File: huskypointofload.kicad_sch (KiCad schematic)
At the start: 8 parts, among them J1 POWER, J2 RFSOC_POWER

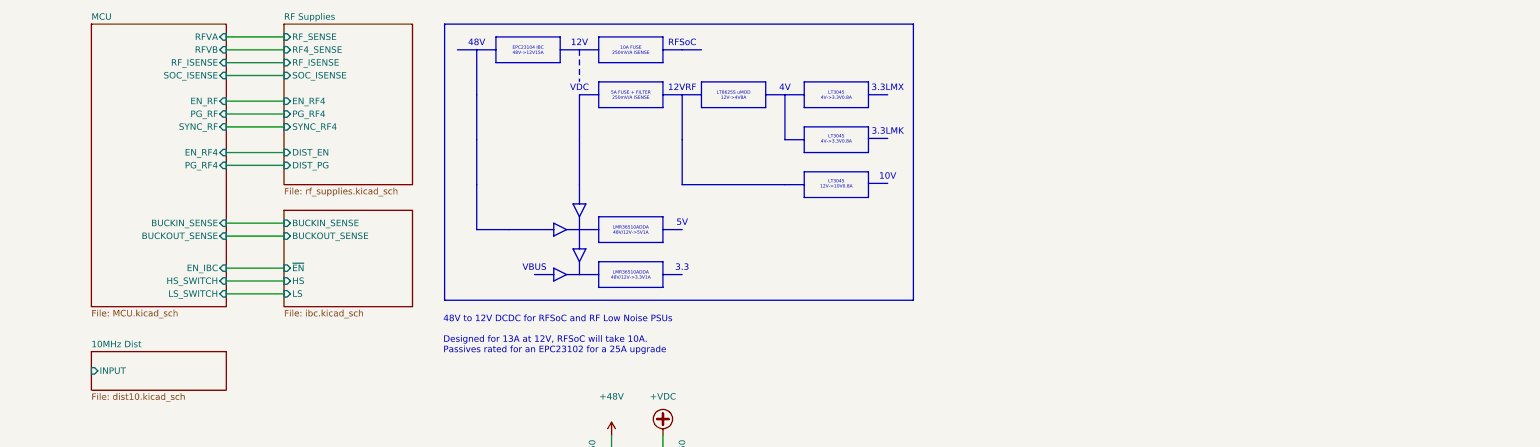
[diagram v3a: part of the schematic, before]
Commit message: Add lmk and bump schematic size
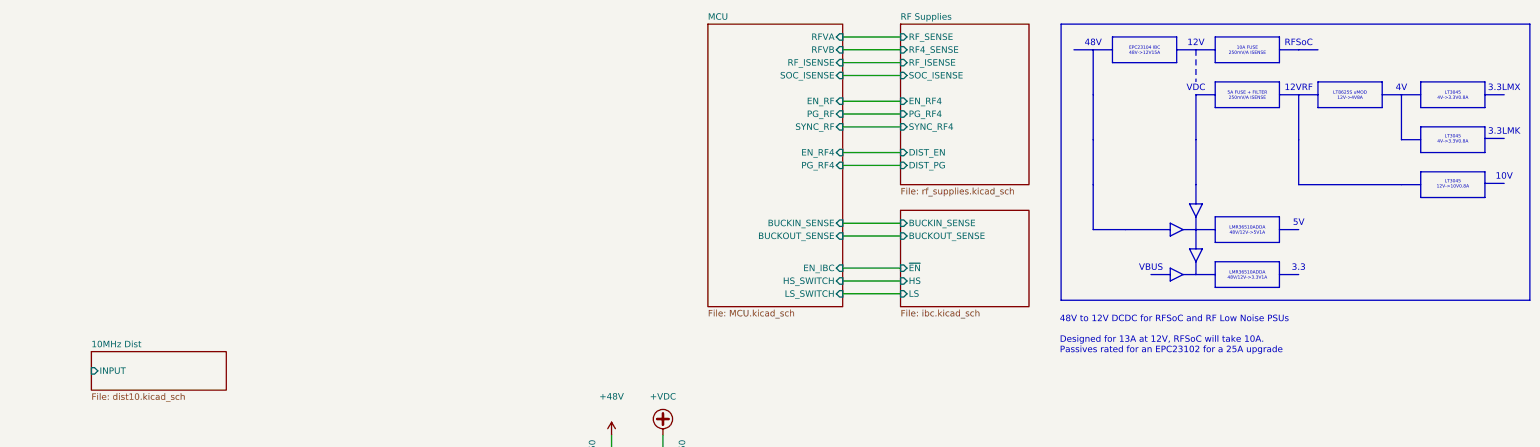
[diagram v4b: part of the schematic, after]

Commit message: Add LMX Draft
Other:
- note added: "3.3LMKDIG"
- note added: "3.3LMKVCO"
- note added: "3.3LMXDIG"
- note added: "3.3LMXPLL"
- note added: "3.3LMXVCO"
- note removed: "3.3LMK"
- note removed: "3.3LMX"

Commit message: Different Matching Circuit
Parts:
- added J39: 10MHZ, symbol Connector:Conn_Coaxial_Small
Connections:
- net 10MHz Dist/INPUT: now also J39.1 (In)
- net GND: now also J39.2 (Ext)
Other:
- sheet Clocking ports: added BACKUP_DIS, LD1, LD2, LD_LED_ENABLE, LMKRESET, LMXCE, MUXOUT, OUTA, OUTB, RAMPCLK, RAMPDIR, SCK, SDIO, SEL0, SEL1, ~{LMKCS}, ~{LMXCS}; removed none
- sheet MCU ports: added BACKUP_DIS, LD1, LD2, LMKRESET, LMXCE, LOCK_LEDS, MISO, MOSI, RAMPCLK, RAMPDIR, SCK, SEL0, SEL1, ~{LMKCS}, ~{LMXCS}; removed none
- moved on the sheet: D1, D2, D3, D4, R1, R2

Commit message: Add mixer
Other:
- added sheet TX Mixer (hmc525.kicad_sch)
- moved on the sheet: J39
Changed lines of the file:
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@@
 	(wire
 		(pts
-			(xy 171.45 95.25) (xy 171.45 97.79)
+			(xy 331.47 29.21) (xy 331.47 31.75)
 		)
 		(stroke
@@
 	(wire
 		(pts
-			(xy 171.45 87.63) (xy 177.8 87.63)
+			(xy 331.47 21.59) (xy 325.12 21.59)
 		)
 		(stroke
@@
 	(wire
 		(pts
-			(xy 171.45 87.63) (xy 171.45 90.17)
+			(xy 331.47 21.59) (xy 331.47 24.13)
 		)
 		(stroke
@@
 	(symbol
 		(lib_id "power:GND")
-		(at 171.45 97.79 0)
+		(at 331.47 31.75 0)
+		(mirror y)
 		(unit 1)
 		(exclude_from_sim no)
@@
 		(fields_autoplaced yes)
 		(property "Reference" "#PWR0263"
-			(at 171.45 104.14 0)
+			(at 331.47 38.1 0)
 			(effects
 				(font
@@
 		)
 		(property "Value" "GND"
-			(at 171.45 102.87 0)
+			(at 331.47 36.83 0)
 			(effects
 				(font
@@
 		)
 		(property "Footprint" ""
-			(at 171.45 97.79 0)
+			(at 331.47 31.75 0)
 			(effects
 				(font
@@
 		)
 		(property "Datasheet" ""
-			(at 171.45 97.79 0)
+			(at 331.47 31.75 0)
 			(effects
 				(font
@@
 		)
 		(property "Description" "Power symbol creates a global label with name \"GND\" , ground"
-			(at 171.45 97.79 0)
+			(at 331.47 31.75 0)
 			(effects
 				(font
@@
 	(symbol
 		(lib_id "Connector:Conn_Coaxial_Small")
-		(at 171.45 92.71 270)
+		(at 331.47 26.67 90)
+		(mirror x)
 		(unit 1)
 		(exclude_from_sim no)
@@
 		(dnp no)
 		(property "Reference" "J39"
-			(at 168.91 90.9203 90)
+			(at 334.01 24.8803 90)
 			(effects
 				(font
@@
 		)
 		(property "Value" "10MHZ"
-			(at 168.91 93.4603 90)
+			(at 334.01 27.4203 90)
 			(effects
 				(font
@@
 		)
 		(property "Footprint" ""
-			(at 171.45 92.71 0)
+			(at 331.47 26.67 0)
 			(effects
 				(font
@@
 		)
 		(property "Datasheet" "~"
-			(at 171.45 92.71 0)
+			(at 331.47 26.67 0)
 			(effects
 				(font
@@
 		)
 		(property "Description" "small coaxial connector (BNC, SMA, SMB, SMC, Cinch/RCA, LEMO, ...)"
-			(at 171.45 92.71 0)
+			(at 331.47 26.67 0)
 			(effects
 				(font
@@
 	)
 	(sheet
-		(at 177.8 83.82)
-		(size 31.75 7.62)
+		(at 298.45 17.78)
+		(size 26.67 7.62)
 		(exclude_from_sim no)
 		(in_bom yes)
@@
 		)
 		(property "Sheetname" "10MHz Dist"
-			(at 177.8 83.1084 0)
+			(at 298.45 17.0684 0)
 			(effects
 				(font
@@
 		)
 		(property "Sheetfile" "dist10.kicad_sch"
-			(at 177.8 92.0246 0)
+			(at 298.45 25.9846 0)
 			(effects
 				(font
@@
 		)
 		(pin "INPUT" input
-			(at 177.8 87.63 180)
+			(at 325.12 21.59 0)
 			(effects
 				(font
 					(size 1.27 1.27)
 				)
-				(justify left)
+				(justify right)
 			)
 		)
@@
 				)
 			)
+		)
+	)
+	(sheet
+		(at 177.8 83.82)
+		(size 25.4 10.16)
+		(exclude_from_sim no)
+		(in_bom yes)
+		(on_board yes)
+		(dnp no)
+		(fields_autoplaced yes)
+		(stroke
+			(width 0.1524)
+			(type solid)
+		)
+		(fill
+			(color 0 0 0 0.0000)
+		)
+		(property "Sheetname" "TX Mixer"
+			(at 177.8 83.1084 0)
+			(effects
+				(font
+					(size 1.27 1.27)
+				)
+				(justify left bottom)
+			)
+		)
+		(property "Sheetfile" "hmc525.kicad_sch"
+			(at 177.8 94.5646 0)
+			(effects
+				(font
+					(size 1.27 1.27)
+				)
+				(justify left top)
+			)
+		)
+		(pin "I" input
+			(at 203.2 86.36 0)
+			(effects
+				(font
+					(size 1.27 1.27)
+				)
+				(justify right)
+			)
+		)
+		(pin "LO" input
+			(at 177.8 86.36 180)
+			(effects
+				(font
+					(size 1.27 1.27)
+				)
+				(justify left)
+			)
+		)
+		(pin "Q" input
+			(at 203.2 88.9 0)
+			(effects
+				(font
+					(size 1.27 1.27)
+				)
+				(justify right)
+			)
+		)
+		(pin "RF" input
+			(at 177.8 88.9 180)
+			(effects
+				(font
+					(size 1.27 1.27)
+				)
+				(justify left)
+			)
+		)
+		(pin "6V" input
+			(at 177.8 91.44 180)
+			(effects
+				(font
+					(size 1.27 1.27)
+				)
+				(justify left)
+			)
+		)
+		(instances
+			(project "huskypointofload"
+				(path "/eb9c972b-d134-41da-be97-ece3f463f7e0"
+					(page "34")
+				)
+			)

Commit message: WIP Splitrail
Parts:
- added U18: ADA4077-1xR, Package_SO:SOIC-8_3.9x4.9mm_P1.27mm, symbol Amplifier_Operational:ADA4077-1xR
- added U27: ADL8124, Package_CSP:LFCSP-8_2x2mm_P0.5mm, symbol huskylib:ADL8124
- added U28: LT3093xMSE, Package_SO:MSOP-12-1EP_3x4.039mm_P0.65mm_EP1.651x2.845mm, symbol Regulator_Linear:LT3093xMSE
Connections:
- new net: U28.1 (IN), U28.13 (IN), U28.2 (IN)
- new net: U28.11 (OUT), U28.12 (OUT)
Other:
- removed sheet Clocking
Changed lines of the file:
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@@
+	)
+	(symbol
+		(lib_id "Regulator_Linear:LT3093xMSE")
+		(at 132.08 138.43 0)
+		(unit 1)
+		(exclude_from_sim no)
+		(in_bom yes)
+		(on_board yes)
+		(dnp no)
+		(fields_autoplaced yes)
+		(property "Reference" "U28"
+			(at 132.08 125.73 0)
+			(effects
+				(font
+					(size 1.27 1.27)
+				)
+			)
+		)
+		(property "Value" "LT3093xMSE"
+			(at 132.08 128.27 0)
+			(effects
+				(font
+					(size 1.27 1.27)
+				)
+			)
+		)
+		(property "Footprint" "Package_SO:MSOP-12-1EP_3x4.039mm_P0.65mm_EP1.651x2.845mm"
+			(at 132.08 127.635 0)
+			(effects
+				(font
+					(size 1.27 1.27)
+				)
+				(hide yes)
+			)
+		)
+		(property "Datasheet" "https://www.analog.com/media/en/technical-documentation/data-sheets/lt3093.pdf"
+			(at 132.08 135.89 0)
+			(effects
+				(font
+					(size 1.27 1.27)
+				)
+				(hide yes)
+			)
+		)
+		(property "Description" "-200mA, Adjustable, Ultralow Noise, Ultrahigh PSRR RF Negative Linear Regulator, MSOP-12"
+			(at 132.08 138.43 0)
+			(effects
+				(font
+					(size 1.27 1.27)
+				)
+				(hide yes)
+			)
+		)
+		(pin "13"
+		)
+		(pin "12"
+		)
+		(pin "1"
+		)
+		(pin "2"
+		)
+		(pin "3"
+		)
+		(pin "4"
+		)
+		(pin "7"
+		)
+		(pin "8"
+		)
+		(pin "9"
+		)
+		(pin "11"
+		)
+		(pin "10"
+		)
+		(pin "5"
+		)
+		(pin "6"
+		)
+		(instances
+			(project ""
+				(path "/eb9c972b-d134-41da-be97-ece3f463f7e0"
+					(reference "U28")
+					(unit 1)
+				)
+			)
+		)
+	)
+	(symbol
+		(lib_id "huskylib:ADL8124")
+		(at 147.32 102.87 0)
+		(unit 1)
+		(exclude_from_sim no)
+		(in_bom yes)
+		(on_board yes)
+		(dnp no)
+		(fields_autoplaced yes)
+		(property "Reference" "U27"
+			(at 135.89 91.948 0)
+			(do_not_autoplace yes)
+			(effects
+				(font
+					(size 1.27 1.27)
+				)
+				(justify left bottom)
+			)
+		)
+		(property "Value" "ADL8124"
+			(at 135.89 93.726 0)
+			(do_not_autoplace yes)
+			(effects
+				(font
+					(size 1.27 1.27)
+				)
+				(justify left bottom)
+			)
+		)
+		(property "Footprint" "Package_CSP:LFCSP-8_2x2mm_P0.5mm"
+			(at 147.32 102.87 0)
+			(effects
+				(font
+					(size 1.27 1.27)
+				)
+				(hide yes)
+			)
+		)
+		(property "Datasheet" "https://www.analog.com/media/en/technical-documentation/data-sheets/adl8124.pdf"
+			(at 147.32 102.87 0)
+			(effects
+				(font
+					(size 1.27 1.27)
+				)
+				(hide yes)
+			)
+		)
+		(property "Description" ""
+			(at 147.32 102.87 0)
+			(effects
+				(font
+					(size 1.27 1.27)
+				)
+				(hide yes)
+			)
+		)
+		(pin "4"
+		)
+		(pin "9"
+		)
+		(pin "4"
+		)
+		(pin "5"
+		)
+		(pin "7"
+		)
+		(pin "1"
+		)
+		(pin "3"
+		)
+		(pin "6"
+		)
+		(pin "8"
+		)
+		(pin "8"
+		)
+		(instances
+			(project ""
+				(path "/eb9c972b-d134-41da-be97-ece3f463f7e0"
+					(reference "U27")
+					(unit 1)
+				)
+			)
+		)
 	)
 	(symbol
@@
 		)
 	)
+	(symbol
+		(lib_id "Amplifier_Operational:ADA4077-1xR")
+		(at 231.14 119.38 0)
+		(unit 1)
+		(exclude_from_sim no)
+		(in_bom yes)
+		(on_board yes)
+		(dnp no)
+		(fields_autoplaced yes)
+		(property "Reference" "U18"
+			(at 243.84 112.9598 0)
+			(effects
+				(font
+					(size 1.27 1.27)
+				)
+			)
+		)
+		(property "Value" "ADA4077-1xR"
+			(at 243.84 115.4998 0)
+			(effects
+				(font
+					(size 1.27 1.27)
+				)
+			)
+		)
+		(property "Footprint" "Package_SO:SOIC-8_3.9x4.9mm_P1.27mm"
+			(at 228.6 124.46 0)
+			(effects
+				(font
+					(size 1.27 1.27)
+				)
+				(justify left)
+				(hide yes)
+			)
+		)
+		(property "Datasheet" "https://www.analog.com/media/en/technical-documentation/data-sheets/ADA4077-1_4077-2_4077-4.pdf"
+			(at 234.95 115.57 0)
+			(effects
+				(font
+					(size 1.27 1.27)
+				)
+				(hide yes)
+			)
+		)
+		(property "Description" "4MHz, 7nV/sqrtHz, Low Offset and Drift, High Precision Amplifier, SOIC-8"
+			(at 231.14 119.38 0)
+			(effects
+				(font
+					(size 1.27 1.27)
+				)
+				(hide yes)
+			)
+		)
+		(pin "6"
+		)
+		(pin "1"
+		)
+		(pin "5"
+		)
+		(pin "4"
+		)
+		(pin "3"
+		)
+		(pin "8"
+		)
+		(pin "7"
+		)
+		(pin "2"
+		)
+		(instances
+			(project ""
+				(path "/eb9c972b-d134-41da-be97-ece3f463f7e0"
+					(reference "U18")
+					(unit 1)
+				)
+			)
+		)
+	)
 	(sheet
 		(at 269.24 17.78)
@@
 				)
 			)
-		)
-	)
-	(sheet
-		(at 177.8 17.78)
-		(size 31.75 55.88)
-		(exclude_from_sim no)
-		(in_bom yes)
-		(on_board yes)
-		(dnp no)
-		(fields_autoplaced yes)
-		(stroke
-			(width 0.1524)
-			(type solid)
-		)
-		(fill
-			(color 0 0 0 0.0000)
-		)
-		(property "Sheetname" "Clocking"
-			(at 177.8 17.0684 0)
-			(effects
-				(font
-					(size 1.27 1.27)
-				)
-				(justify left bottom)
-			)
-		)
-		(property "Sheetfile" "clocking.kicad_sch"
-			(at 177.8 74.2446 0)
-			(effects
-				(font
-					(size 1.27 1.27)
-				)
-				(justify left top)
-			)
-		)
-		(pin "BACKUP_DIS" input
-			(at 209.55 53.34 0)
-			(effects
-				(font
-					(size 1.27 1.27)
-				)
-				(justify right)
-			)
-		)
-		(pin "LD1" input
-			(at 209.55 58.42 0)
-			(effects
-				(font
-					(size 1.27 1.27)
-				)
-				(justify right)
-			)
-		)
-		(pin "LD2" input
-			(at 209.55 60.96 0)
-			(effects
-				(font
-					(size 1.27 1.27)
-				)
-				(justify right)
-			)
-		)
-		(pin "LD_LED_ENABLE" input
-			(at 209.55 66.04 0)
-			(effects
-				(font
-					(size 1.27 1.27)
-				)
-				(justify right)
-			)
-		)
-		(pin "LMKRESET" input
-			(at 209.55 20.32 0)
-			(effects
-				(font
-					(size 1.27 1.27)
-				)
-				(justify right)
-			)
-		)
-		(pin "LMXCE" input
-			(at 209.55 22.86 0)
-			(effects
-				(font
-					(size 1.27 1.27)
-				)
-				(justify right)
-			)
-		)
-		(pin "MUXOUT" input
-			(at 209.55 63.5 0)
-			(effects
-				(font
-					(size 1.27 1.27)
-				)
-				(justify right)
-			)
-		)
-		(pin "OUTA" input
-			(at 177.8 20.32 180)
-			(effects
-				(font
-					(size 1.27 1.27)
-				)
-				(justify left)
-			)
-		)
-		(pin "OUTB" input
-			(at 177.8 22.86 180)
-			(effects
-				(font
-					(size 1.27 1.27)
-				)
-				(justify left)
-			)
-		)
-		(pin "RAMPCLK" input
-			(at 209.55 43.18 0)
-			(effects
-				(font
-					(size 1.27 1.27)
-				)
-				(justify right)
-			)
-		)
-		(pin "RAMPDIR" input
-			(at 209.55 40.64 0)
-			(effects
-				(font
-					(size 1.27 1.27)
-				)
-				(justify right)
-			)
-		)
-		(pin "SCK" input
-			(at 209.55 33.02 0)
-			(effects
-				(font
-					(size 1.27 1.27)
-				)
-				(justify right)
-			)
-		)
-		(pin "SDIO" input
-			(at 209.55 35.56 0)
-			(effects
-				(font
-					(size 1.27 1.27)
-				)
-				(justify right)
-			)
-		)
-		(pin "SEL0" input
-			(at 209.55 48.26 0)
-			(effects
-				(font
-					(size 1.27 1.27)
-				)
-				(justify right)
-			)
-		)
-		(pin "SEL1" input
-			(at 209.55 50.8 0)
-			(effects
-				(font
-					(size 1.27 1.27)
-				)
-				(justify right)
-			)
-		)
-		(pin "~{LMKCS}" input
-			(at 209.55 27.94 0)
-			(effects
-				(font
-					(size 1.27 1.27)
-				)
-				(justify right)
-			)
-		)
-		(pin "~{LMXCS}" input
-			(at 209.55 30.48 0)
-			(effects
-				(font
-					(size 1.27 1.27)
-				)
-				(justify right)
-			)
-		)
-		(instances
-			(project "huskypointofload"
-				(path "/eb9c972b-d134-41da-be97-ece3f463f7e0"
-					(page "16")
-				)
-			)
